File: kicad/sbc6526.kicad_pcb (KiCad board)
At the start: 4 copper layers, 100 x 100 mm, 59 parts, among them P1 2k, P2 5k, SW1 UP, SW2 DOWN, SW3 OK, SW4 CANCEL, SW5 RESET, U1 6526, U10 74AC138, U11 74ACT245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

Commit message: v2.0
Production ready
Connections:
- net D0 renamed /D0
- net D1 renamed /D1
- net D2 renamed /D2
- net D3 renamed /D3
- net D4 renamed /D4
- net D5 renamed /D5
- net D6 renamed /D6
- net D7 renamed /D7
- LCD1 pad : GND -> (no net)
- U4 pad 1: (no net) -> no_connect_146
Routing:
- net /A0: track 177.9 -> 172.8 mm
- net /A1: track 167.4 -> 165.2 mm
- net /PHI2: track 148.8 -> 147.5 mm
- net /A2: track 163.5 -> 162.6 mm

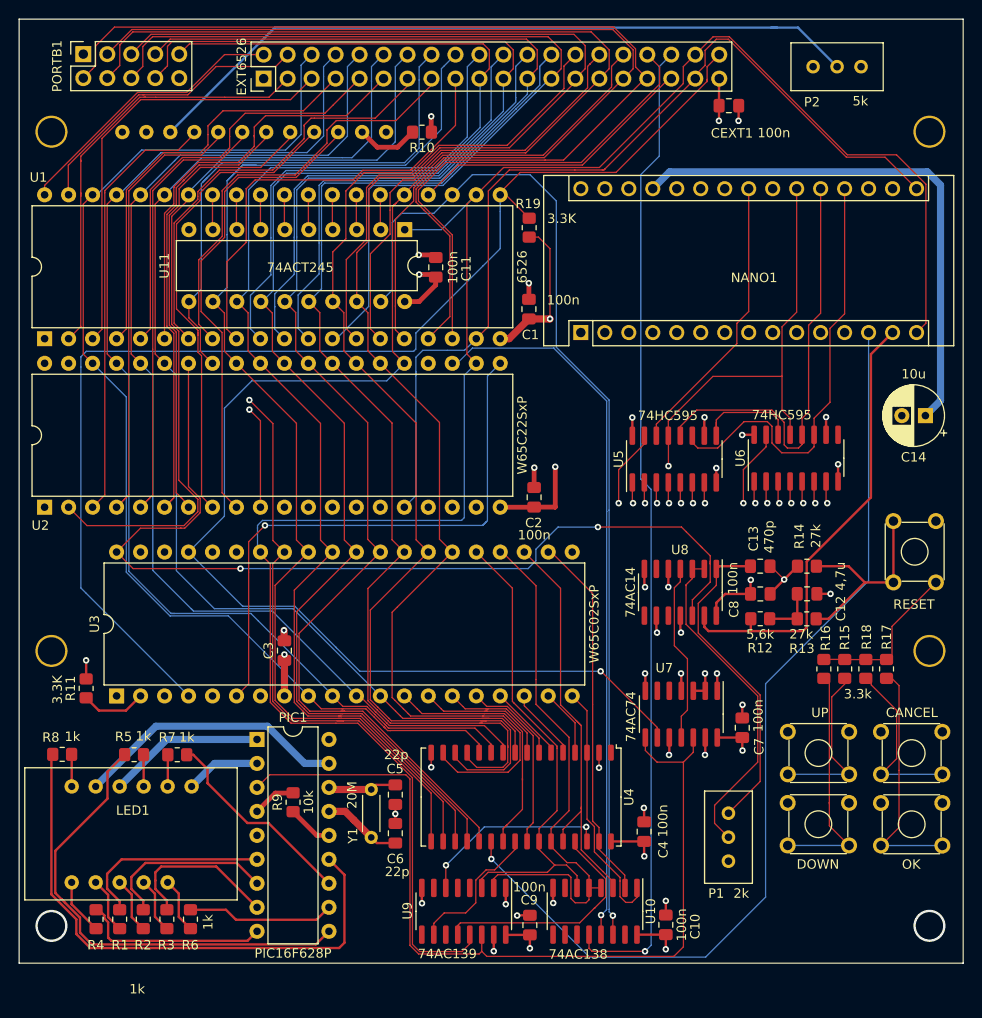
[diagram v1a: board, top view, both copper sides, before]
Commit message: v2.0 layout optimization
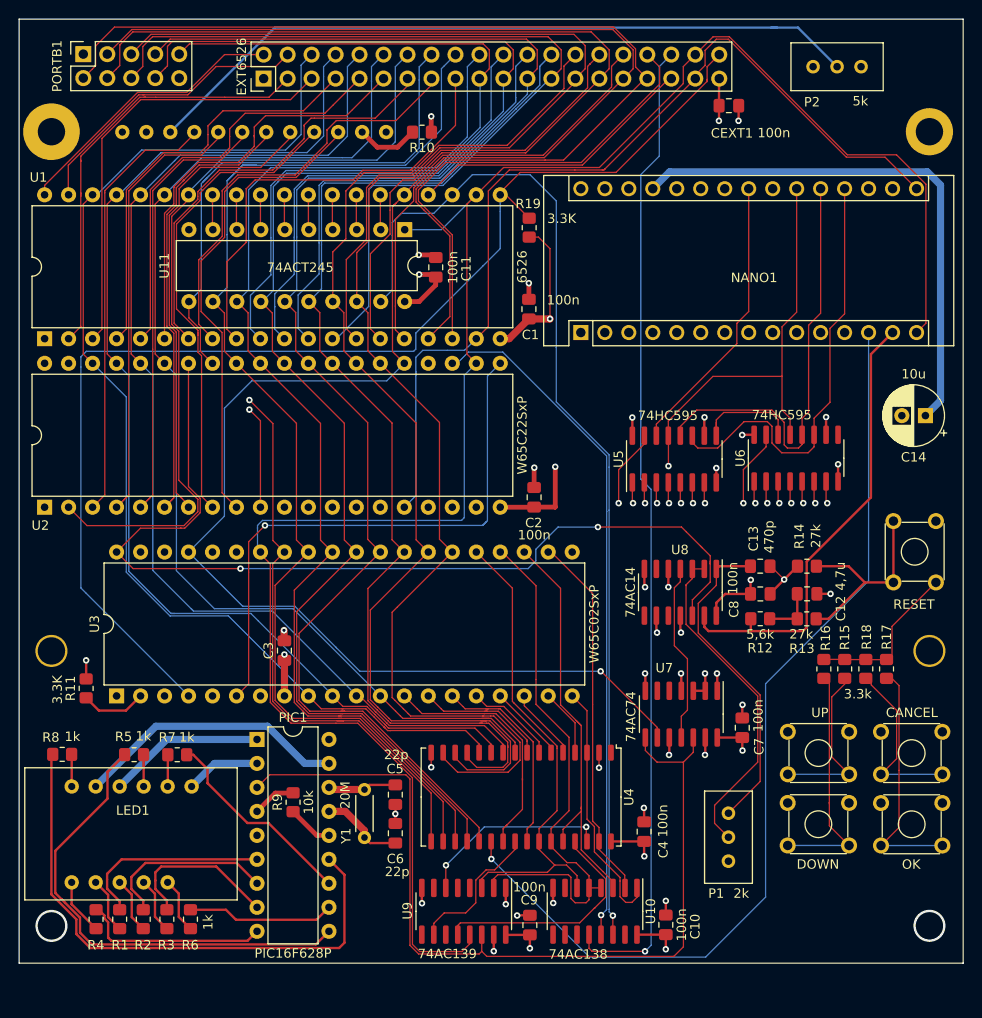
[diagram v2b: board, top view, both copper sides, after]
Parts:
- moved Y1 0.72 mm to (136.6, 131.6)
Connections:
- LCD1 pad : (no net) -> GND
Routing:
- net /~VIA: track 76.1 -> 72.4 mm
- net /D5: track 162.7 -> 162.0 mm
- net /D6: track 160.2 -> 159.5 mm
- net /A3: track 160.9 -> 160.2 mm
- net /D7: track 155.4 -> 154.8 mm
- net /A4: track 65.9 -> 65.3 mm

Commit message: Minor fixes in PCB, and ready for production
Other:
- board text added: "sbc6526 v2.0.1"
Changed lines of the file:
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@@
       (drillshape 0)
       (scaleselection 1)
-      (outputdirectory "")
+      (outputdirectory "Gerber/")
     )
   )
@@
   (gr_line (start 200 150) (end 200 50) (layer "Edge.Cuts") (width 0.05))
   (gr_line (start 100 50) (end 100 150) (layer "Edge.Cuts") (width 0.05))
+  (gr_text "sbc6526 v2.0.1" (at 183.475 146.05) (layer "F.SilkS")
+    (effects (font (size 1.5 1.5) (thickness 0.2) italic))
+  )
   (segment (start 118.930501 100.870501) (end 118.930501 102.175441) (width 0.127) (layer "F.Cu") (net 1))
   (segment (start 116.16203 70.890642) (end 116.16203 82.318582) (width 0.127) (layer "F.Cu") (net 1))

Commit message: Fixes to mounting holes.
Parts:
- added VCC1: VCC, MountingHole:MountingHole_2.2mm_M2_DIN965_Pad, F.Cu at (195.9, 146.4)
- added VCC2: VCC, MountingHole:MountingHole_2.2mm_M2_DIN965_Pad, F.Cu at (103.4, 146.1)
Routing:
- net VCC: track 191.2 -> 167.3 mm, vias 23 -> 21
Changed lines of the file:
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@@
   )
   (setup
+    (stackup
+      (layer "F.SilkS" (type "Top Silk Screen"))
+      (layer "F.Paste" (type "Top Solder Paste"))
+      (layer "F.Mask" (type "Top Solder Mask") (color "Green") (thickness 0.01))
+      (layer "F.Cu" (type "copper") (thickness 0.035))
+      (layer "dielectric 1" (type "core") (thickness 0.480066) (material "FR4") (epsilon_r 4.5) (loss_tangent 0.02))
+      (layer "In1.Cu" (type "copper") (thickness 0.035))
+      (layer "dielectric 2" (type "prepreg") (thickness 0.480066) (material "FR4") (epsilon_r 4.5) (loss_tangent 0.02))
+      (layer "In2.Cu" (type "copper") (thickness 0.035))
+      (layer "dielectric 3" (type "core") (thickness 0.480066) (material "FR4") (epsilon_r 4.5) (loss_tangent 0.02))
+      (layer "B.Cu" (type "copper") (thickness 0.035))
+      (layer "B.Mask" (type "Bottom Solder Mask") (color "Green") (thickness 0.01))
+      (layer "B.Paste" (type "Bottom Solder Paste"))
+      (layer "B.SilkS" (type "Bottom Silk Screen"))
+      (copper_finish "None")
+      (dielectric_constraints no)
+    )
     (pcbplotparams
       (layerselection 0x00010fc_ffffffff)
@@
       (effects (font (size 1 1) (thickness 0.15)))
     )
-    (fp_text value "100n" (at 0 1.68 90) (layer "F.Fab")
+    (fp_text value "100n" (at 0 1.68 90) (layer "F.SilkS")
       (effects (font (size 1 1) (thickness 0.15)))
     )
@@
       (effects (font (size 1 1) (thickness 0.15)))
     )
-    (fp_text value "330" (at 0 1.65) (layer "F.Fab")
+    (fp_text value "330" (at 0 1.65) (layer "F.SilkS")
       (effects (font (size 1 1) (thickness 0.15)))
     )
@@
       (effects (font (size 1 1) (thickness 0.15)))
     )
-    (pad "" thru_hole circle (at 46.5 -27.5) (size 5 5) (drill 2.9) (layers *.Cu *.Mask)
+    (pad "" thru_hole circle (at 46.5 -27.5) (size 3.8 3.8) (drill 2.2) (layers *.Cu *.Mask)
       (net 4 "GND") (zone_connect 2))
     (pad "" thru_hole circle (at 46.5 27.5) (size 3.4 3.4) (drill 2.9) (layers *.Cu *.Mask)
@@
     (pad "" thru_hole circle (at -46.5 27.5) (size 3.4 3.4) (drill 2.9) (layers *.Cu *.Mask)
       (zone_connect 2))
-    (pad "" thru_hole circle (at -46.5 -27.5) (size 6 6) (drill 2.9) (layers *.Cu *.Mask)
+    (pad "" thru_hole circle (at -46.5 -27.5) (size 3.8 3.8) (drill 2.2) (layers *.Cu *.Mask)
       (net 4 "GND") (zone_connect 2))
     (pad "1" thru_hole circle (at -38.99 -27.46) (size 1.524 1.524) (drill 0.762) (layers *.Cu *.Mask)
@@
     )
   )
+  (footprint "MountingHole:MountingHole_2.2mm_M2_DIN965_Pad" (layer "F.Cu")
+    (at 103.425 146.05)
+    (descr "Mounting Hole 2.2mm, M2, DIN965")
+    (tags "mounting hole 2.2mm m2 din965")
+    (zone_connect 2)
+    (attr board_only exclude_from_pos_files exclude_from_bom)
+    (fp_text reference "VCC2" (at 0 -2.9) (layer "F.SilkS") hide
+      (effects (font (size 1 1) (thickness 0.15)))
+    )
+    (fp_text value "VCC" (at 0 2.9) (layer "F.SilkS")
+      (effects (font (size 1 1) (thickness 0.15)))
+    )
+    (fp_text user "${REFERENCE}" (at 0.3 0) (layer "F.Fab") hide
+      (effects (font (size 1 1) (thickness 0.15)))
+    )
+    (fp_circle (center 0 0) (end 1.9 0) (layer "Cmts.User") (width 0.15) (fill none))
+    (fp_circle (center 0 0) (end 2.15 0) (layer "F.CrtYd") (width 0.05) (fill none))
+    (pad "VCC" thru_hole circle (at 0 0) (size 3.8 3.8) (drill 2.2) (layers *.Cu *.Mask)
+      (net 8 "VCC") (zone_connect 2))
+  )
   (footprint "Connector_PinSocket_2.54mm:PinSocket_2x05_P2.54mm_Vertical" (layer "F.Cu")
     (at 106.8 53.71 90)
@@
     )
   )
+  (footprint "MountingHole:MountingHole_2.2mm_M2_DIN965_Pad" (layer "F.Cu")
+    (at 195.9 146.425)
+    (descr "Mounting Hole 2.2mm, M2, DIN965")
+    (tags "mounting hole 2.2mm m2 din965")
+    (zone_connect 2)
+    (attr board_only exclude_from_pos_files exclude_from_bom)
+    (fp_text reference "VCC1" (at 0 -2.9) (layer "F.SilkS") hide
+      (effects (font (size 1 1) (thickness 0.15)))
+    )
+    (fp_text value "VCC" (at -0.05 -2.95) (layer "F.SilkS")
+      (effects (font (size 1 1) (thickness 0.15)))
+    )
+    (fp_text user "${REFERENCE}" (at 0.3 0) (layer "F.Fab") hide
+      (effects (font (size 1 1) (thickness 0.15)))
+    )
+    (fp_circle (center 0 0) (end 1.9 0) (layer "Cmts.User") (width 0.15) (fill none))
+    (fp_circle (center 0 0) (end 2.15 0) (layer "F.CrtYd") (width 0.05) (fill none))
+    (pad "VCC" thru_hole circle (at 0 -0.375) (size 3.8 3.8) (drill 2.2) (layers *.Cu *.Mask)
+      (net 8 "VCC") (zone_connect 2))
+  )
   (gr_line (start 200 50) (end 100 50) (layer "Edge.Cuts") (width 0.05))
   (gr_line (start 100 150) (end 200 150) (layer "Edge.Cuts") (width 0.05))
@@
   (via (at 177.5 109.4) (size 0.6858) (drill 0.3302) (layers "F.Cu" "B.Cu") (net 8))
   (via (at 174.125 60.775) (size 0.6858) (drill 0.3302) (layers "F.Cu" "B.Cu") (net 8))
-  (via (at 196.425 146.04) (size 3.4) (drill 2.9) (layers "F.Cu" "B.Cu") (net 8))
   (via (at 154.1 148.425) (size 0.6858) (drill 0.3302) (layers "F.Cu" "B.Cu") (net 8))
   (via (at 168.84 127.941) (size 0.6858) (drill 0.3302) (layers "F.Cu" "B.Cu") (net 8))
@@
   (via (at 156.79 97.42) (size 0.6858) (drill 0.3302) (layers "F.Cu" "B.Cu") (net 8))
   (via (at 176.58709 94.047954) (size 0.6858) (drill 0.3302) (layers "F.Cu" "B.Cu") (net 8))
-  (via (at 103.425 146.05) (size 3.4) (drill 2.9) (layers "F.Cu" "B.Cu") (net 8))
   (via (at 164.95 92.2) (size 0.6858) (drill 0.3302) (layers "F.Cu" "B.Cu") (net 8))
   (via (at 172.65 127.941) (size 0.6858) (drill 0.3302) (layers "F.Cu" "B.Cu") (net 8))
   (via (at 107.1 117.92) (size 0.6858) (drill 0.3302) (layers "F.Cu" "B.Cu") (net 8))
-  (segment (start 103.425 146.05) (end 103.43 146.055) (width 0.254) (layer "In1.Cu") (net 8))
-  (segment (start 103.425 146.05) (end 103.425 147.775) (width 0.762) (layer "In2.Cu") (net 8))
-  (segment (start 196.455 146.07) (end 196.515 146.01) (width 0.762) (layer "In2.Cu") (net 8))
-  (segment (start 101.42 146.05) (end 100.93 146.54) (width 0.762) (layer "In2.Cu") (net 8))
   (segment (start 143.34 85.135) (end 142.31 85.135) (width 0.254) (layer "In2.Cu") (net 8))
-  (segment (start 106.14 146.05) (end 106.77 146.68) (width 0.762) (layer "In2.Cu") (net 8))
-  (segment (start 103.425 146.05) (end 106.14 146.05) (width 0.762) (layer "In2.Cu") (net 8))
-  (segment (start 103.425 144.215) (end 102.57 143.36) (width 0.762) (layer "In2.Cu") (net 8))
-  (segment (start 196.515 146.01) (end 198.64 146.01) (width 0.762) (layer "In2.Cu") (net 8))
-  (segment (start 196.425 146.04) (end 196.455 146.07) (width 0.762) (layer "In2.Cu") (net 8))
   (segment (start 143.34 86.46) (end 143.34 85.135) (width 0.254) (layer "In2.Cu") (net 8))
-  (segment (start 196.425 148.565) (end 196.425 146.04) (width 0.762) (layer "In2.Cu") (net 8))
-  (segment (start 103.425 146.05) (end 101.42 146.05) (width 0.762) (layer "In2.Cu") (net 8))
-  (segment (start 103.425 147.775) (end 104.39 148.74) (width 0.762) (layer "In2.Cu") (net 8))
-  (segment (start 196.425 143.315) (end 196.425 146.04) (width 0.762) (layer "In2.Cu") (net 8))
-  (segment (start 103.425 146.05) (end 103.425 144.215) (width 0.762) (layer "In2.Cu") (net 8))
-  (segment (start 192.5 146.04) (end 196.425 146.04) (width 0.762) (layer "In2.Cu") (net 8))
   (segment (start 197.6 67.575) (end 197.6 90.4) (width 0.762) (layer "B.Cu") (net 8))
   (segment (start 140.8 79.877) (end 140.843 79.92) (width 0.762) (layer "B.Cu") (net 8))
@@
   (segment (start 150.96 68.61) (end 151.55 68.61) (width 0.127) (layer "F.Cu") (net 40))
   (segment (start 163.219942 66.24) (end 172.875 56.584942) (width 0.127) (layer "F.Cu") (net 40))
-  (segment (start 172.875 56.635) (end 172.875 56.395) (width 0.127) (layer "F.Cu") (net 40))
   (segment (start 150.96 68.36) (end 153.08 66.24) (width 0.127) (layer "F.Cu") (net 40))
   (segment (start 163.05 66.24) (end 163.219942 66.24) (width 0.127) (layer "F.Cu") (net 40))

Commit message: v2
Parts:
- U2: value W65C22SxP -> W65C22S
- U3: value W65C02SxP -> W65C02S
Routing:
- net Net-(PIC1-Pad10): track 50.4 -> 49.0 mm
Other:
- board text added: "sbc6526 v2.0.0"
- board text removed: "sbc6526 v2.0.1"
